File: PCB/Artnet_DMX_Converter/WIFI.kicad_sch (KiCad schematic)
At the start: 1 part, among them J13 Conn_02x04

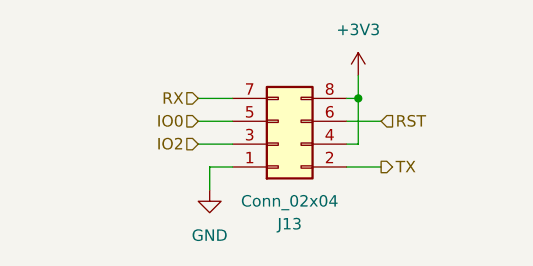
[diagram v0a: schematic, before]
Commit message: Updated the PCB Allot
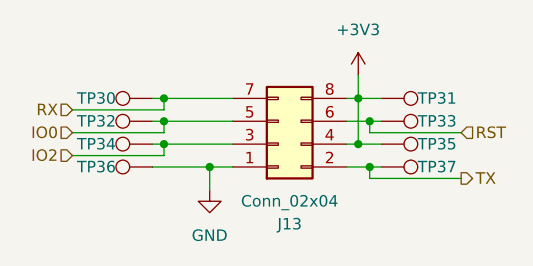
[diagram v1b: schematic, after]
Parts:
- added TP30, TP31, TP32, TP33, TP34, TP35, TP36, TP37: TestPoint, TestPoint:TestPoint_Pad_D1.5mm, symbol Connector:TestPoint
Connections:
- net +3V3: now also TP31.1, TP35.1
- net GND: now also TP36.1
- net IO0: now also TP32.1
- net IO2: now also TP34.1
- net RST: now also TP33.1
- net RX: now also TP30.1
- net TX: now also TP37.1
